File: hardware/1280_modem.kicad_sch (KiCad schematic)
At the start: 73 parts, among them IC1 SX1281IMLTRT, IC2 SKY65383-11, IC3 TJA1462AT_0Z, J2 Conn_Coaxial, J2 jst gh 4, J5 jst gh 6, J8 USB_C_Receptacle_USB2.0, J9 jst_sh 6, U13 STM32U575CGTx, U2 TPS7A20285PDBVR, U2 USBLC6-2SC6, Y1 48MHz, Y1 52MHz

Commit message: improvements
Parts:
- added C30, C31: 1u, Capacitor_SMD:C_0603_1608Metric, symbol Device:C_Small
- added D4: MBR1020VL, Diode_SMD:D_SOD-323_HandSoldering, symbol Device:D_Small
- added D5, D6, D7, D8: SZNUP2105L, Package_TO_SOT_SMD:SOT-23, symbol Power_Protection:SZNUP2105L
- added JP1: SolderJumper_2_Open, Jumper:SolderJumper-2_P1.3mm_Open_TrianglePad1.0x1.5mm, symbol Jumper:SolderJumper_2_Open
- added U4: TPS7A2450DBVR, Package_TO_SOT_SMD:SOT-23-5, symbol Regulator_Linear:TPS7A0525PDBV
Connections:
- net +5V: now also C31.1, U4.5 (OUT); no longer C2.2, C5.1, J2.1 (Pin_1), J5.1 (Pin_1), J8.A4 (VBUS), J8.A9 (VBUS), J8.B4 (VBUS), J8.B9 (VBUS), PS1.1 (VIN_1), PS1.2 (VIN_2), PS1.3 (EN), U2.5 (VBUS)
- net CAN_H: now also D5.2 (K)
- net CAN_L: now also D5.1 (K), JP1.2 (B); no longer R18.2
- net Earth: now also C30.1, C31.2, D5.3 (A), D6.3 (A), D7.3 (A), D8.3 (A), U4.2 (GND)
- net UART_CTS: now also D7.2 (K)
- net UART_RTS: now also D7.1 (K)
- net UART_RX: now also D6.1 (K)
- net UART_TX: now also D6.2 (K)
- new net: JP1.1 (A), R18.2
- new net VBUS: D4.2 (A), J8.A4 (VBUS), J8.A9 (VBUS), J8.B4 (VBUS), J8.B9 (VBUS), U2.5 (VBUS)
- new net VCC: C2.2, C30.2, C5.1, D4.1 (K), D8.1 (K), D8.2 (K), J2.1 (Pin_1), J5.1 (Pin_1), PS1.1 (VIN_1), PS1.2 (VIN_2), PS1.3 (EN), U4.1 (IN), U4.3 (EN)
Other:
- note added: "USB in -> 5.2v diode drop -> 4.9v ldo drop -> 4.7v"
- moved on the sheet: D1, D2, IC3, R11, R12, R18

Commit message: stuff
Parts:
- removed D3: pwr, LED_SMD:LED_0805_2012Metric, symbol Device:LED_Small
- removed R13: 330, Resistor_SMD:R_0603_1608Metric, symbol Device:R_Small
- added D9: IN-S128TATRGB, LED_SMD:LED_RGB_1210, symbol Device:LED_ARGB
- added R19: 330, Resistor_SMD:R_0603_1608Metric, symbol Device:R_Small
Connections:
- net +3V3: now also R19.2
- net Earth: now also D9.2 (RK)
- net LED_G: now reaches U13.20 (PB2)
- net LED_G: now also D9.3 (GK)
- net LED_B: now reaches U13.27 (PB14)
- net LED_B: now also D9.4 (BK)
- new net: D9.1 (A), R19.1
- no-connect marks 16 -> 14

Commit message: prettier schematic
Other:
- note added: "CONNECTORS"
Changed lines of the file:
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@@
     (fill (type none))
   )
-  (rectangle (start 19.05 180.34) (end 139.7 279.4)
+  (rectangle (start 19.05 180.34) (end 147.32 279.4)
     (stroke (width 0) (type default))
     (fill (type none))
@@
     (effects (font (size 1.27 1.27)) (justify left bottom))
   )
-  (text "CAN" (at 349.25 74.93 0)
+  (text "CONNECTORS" (at 349.25 74.93 0)
     (effects (font (size 1.27 1.27)) (justify left bottom))
   )

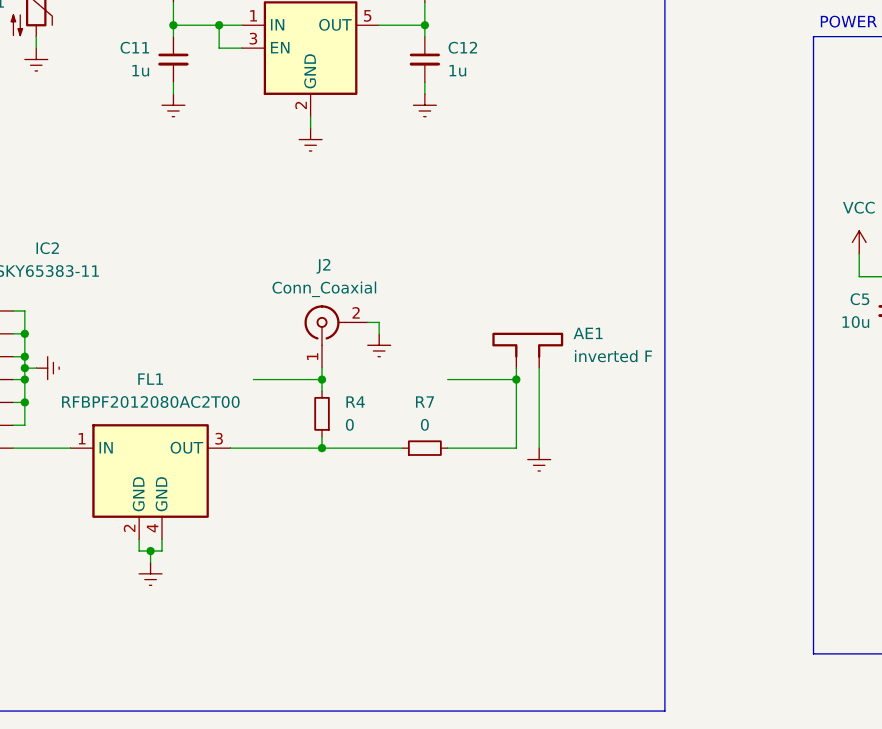
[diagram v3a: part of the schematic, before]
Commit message: micro strip and antenna tuning
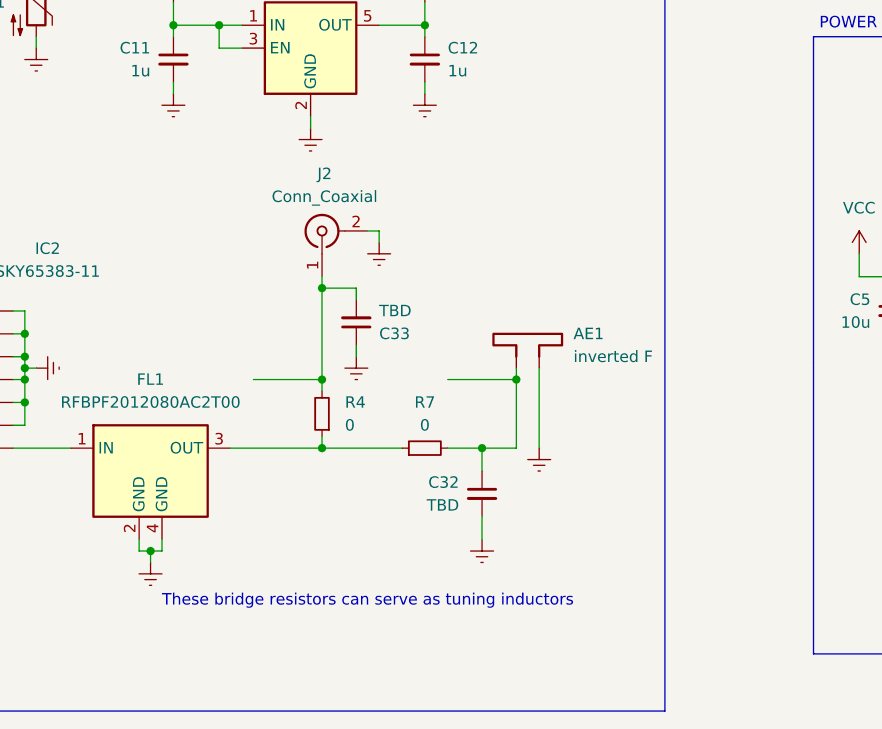
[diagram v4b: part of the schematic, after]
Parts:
- added C32, C33: TBD, Capacitor_SMD:C_0402_1005Metric, symbol Device:C_Small
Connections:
- net Earth: now also C32.2, C33.1
- net at AE1.1, R7.2: now also C32.1
- net at J2.1 (In), R4.2: now also C33.2
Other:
- note added: "These bridge resistors can serve as tuning inductors"
- moved on the sheet: J2
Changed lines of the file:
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@@
   (junction (at 22.86 198.12) (diameter 0) (color 0 0 0 0)
   )
+  (junction (at 127 250.19) (diameter 0) (color 0 0 0 0)
+  )
   (junction (at 69.85 119.38) (diameter 0) (color 0 0 0 0)
   )
+  (junction (at 109.22 232.41) (diameter 0) (color 0 0 0 0)
+  )
   (junction (at 76.2 240.03) (diameter 0) (color 0 0 0 0)
   )
@@
     (stroke (width 0) (type default))
   )
+  (wire (pts (xy 127 250.19) (xy 127 252.73))
+    (stroke (width 0) (type default))
+  )
   (wire (pts (xy 24.13 273.05) (xy 24.13 271.78))
     (stroke (width 0) (type default))
@@
     (stroke (width 0) (type default))
   )
+  (wire (pts (xy 109.22 232.41) (xy 113.03 232.41))
+    (stroke (width 0) (type default))
+  )
   (wire (pts (xy 120.65 203.2) (xy 120.65 204.47))
     (stroke (width 0) (type default))
@@
     (stroke (width 0) (type default))
   )
+  (wire (pts (xy 109.22 232.41) (xy 109.22 242.57))
+    (stroke (width 0) (type default))
+  )
   (wire (pts (xy 177.8 149.86) (xy 177.8 147.32))
     (stroke (width 0) (type default))
@@
     (stroke (width 0) (type default))
   )
-  (wire (pts (xy 109.22 241.3) (xy 109.22 242.57))
+  (wire (pts (xy 109.22 231.14) (xy 109.22 232.41))
     (stroke (width 0) (type default))
   )
@@
     (stroke (width 0) (type default))
   )
+  (wire (pts (xy 127 250.19) (xy 130.81 250.19))
+    (stroke (width 0) (type default))
+  )
   (wire (pts (xy 231.14 241.3) (xy 233.68 241.3))
     (stroke (width 0) (type default))
@@
     (stroke (width 0) (type default))
   )
+  (wire (pts (xy 127 257.81) (xy 127 260.35))
+    (stroke (width 0) (type default))
+  )
   (wire (pts (xy 364.49 46.99) (xy 373.38 46.99))
     (stroke (width 0) (type default))
@@
     (stroke (width 0) (type default))
   )
+  (wire (pts (xy 113.03 233.68) (xy 113.03 232.41))
+    (stroke (width 0) (type default))
+  )
   (wire (pts (xy 220.98 101.6) (xy 236.22 101.6))
     (stroke (width 0) (type default))
@@
     (stroke (width 0) (type default))
   )
-  (wire (pts (xy 123.19 250.19) (xy 130.81 250.19))
+  (wire (pts (xy 123.19 250.19) (xy 127 250.19))
     (stroke (width 0) (type default))
   )
@@
     (stroke (width 0) (type default))
   )
-  (wire (pts (xy 114.3 236.22) (xy 115.57 236.22))
+  (wire (pts (xy 114.3 226.06) (xy 115.57 226.06))
     (stroke (width 0) (type default))
   )
@@
     (stroke (width 0) (type default))
   )
-  (wire (pts (xy 115.57 236.22) (xy 115.57 237.49))
+  (wire (pts (xy 115.57 226.06) (xy 115.57 227.33))
     (stroke (width 0) (type default))
   )
@@
     (stroke (width 0) (type default))
   )
+  (wire (pts (xy 113.03 238.76) (xy 113.03 240.03))
+    (stroke (width 0) (type default))
+  )
   (wire (pts (xy 71.12 118.11) (xy 71.12 119.38))
     (stroke (width 0) (type default))
@@
     (effects (font (size 1.27 1.27)) (justify left bottom))
   )
+  (text "These bridge resistors can serve as tuning inductors"
+    (at 91.44 267.97 0)
+    (effects (font (size 1.27 1.27)) (justify left bottom))
+  )
   (text "Frontend" (at 182.88 199.39 0)
     (effects (font (size 1.27 1.27)) (justify left bottom))
@@
     )
   )
-  (symbol (lib_name "Earth_20") (lib_id "power:Earth") (at 115.57 237.49 0) (unit 1)
+  (symbol (lib_name "Earth_20") (lib_id "power:Earth") (at 115.57 227.33 0) (unit 1)
     (in_bom yes) (on_board yes) (dnp no) (fields_autoplaced)
-    (property "Reference" "#PWR035" (at 115.57 243.84 0)
+    (property "Reference" "#PWR035" (at 115.57 233.68 0)
       (effects (font (size 1.27 1.27)) hide)
     )
-    (property "Value" "Earth" (at 115.57 241.3 0)
+    (property "Value" "Earth" (at 115.57 231.14 0)
       (effects (font (size 1.27 1.27)) hide)
     )
-    (property "Footprint" "" (at 115.57 237.49 0)
+    (property "Footprint" "" (at 115.57 227.33 0)
       (effects (font (size 1.27 1.27)) hide)
     )
-    (property "Datasheet" "~" (at 115.57 237.49 0)
+    (property "Datasheet" "~" (at 115.57 227.33 0)
       (effects (font (size 1.27 1.27)) hide)
     )
@@
     )
   )
+  (symbol (lib_id "Device:C_Small") (at 127 255.27 0) (mirror y) (unit 1)
+    (in_bom yes) (on_board yes) (dnp no)
+    (property "Reference" "C32" (at 124.46 254.0063 0)
+      (effects (font (size 1.27 1.27)) (justify left))
+    )
+    (property "Value" "TBD" (at 124.46 256.5463 0)
+      (effects (font (size 1.27 1.27)) (justify left))
+    )
+    (property "Footprint" "Capacitor_SMD:C_0402_1005Metric" (at 127 255.27 0)
+      (effects (font (size 1.27 1.27)) hide)
+    )
+    (property "Datasheet" "~" (at 127 255.27 0)
+      (effects (font (size 1.27 1.27)) hide)
+    )
+    (pin "1")
+    (pin "2")
+    (instances
+      (project "1280_modem"
+        (path "/f19b1dac-2dd5-424b-bd9e-1e3b3f325373"
+          (reference "C32") (unit 1)
+        )
+      )
+    )
+  )
   (symbol (lib_id "power:+3.3VA") (at 41.91 264.16 0) (unit 1)
     (in_bom yes) (on_board yes) (dnp no) (fields_autoplaced)
@@
     )
   )
+  (symbol (lib_name "Earth_44") (lib_id "power:Earth") (at 113.03 240.03 0) (unit 1)
+    (in_bom yes) (on_board yes) (dnp no) (fields_autoplaced)
+    (property "Reference" "#PWR084" (at 113.03 246.38 0)
+      (effects (font (size 1.27 1.27)) hide)
+    )
+    (property "Value" "Earth" (at 113.03 243.84 0)
+      (effects (font (size 1.27 1.27)) hide)
+    )
+    (property "Footprint" "" (at 113.03 240.03 0)
+      (effects (font (size 1.27 1.27)) hide)
+    )
+    (property "Datasheet" "~" (at 113.03 240.03 0)
+      (effects (font (size 1.27 1.27)) hide)
+    )
+    (pin "1")
+    (instances
+      (project "1280_modem"
+        (path "/f19b1dac-2dd5-424b-bd9e-1e3b3f325373"
+          (reference "#PWR084") (unit 1)
+        )
+      )
+    )
+  )
   (symbol (lib_name "Earth_12") (lib_id "power:Earth") (at 350.52 205.105 0) (unit 1)
     (in_bom yes) (on_board yes) (dnp no) (fields_autoplaced)
@@
     )
   )
+  (symbol (lib_id "Device:C_Small") (at 113.03 236.22 0) (mirror x) (unit 1)
+    (in_bom yes) (on_board yes) (dnp no)
+    (property "Reference" "C33" (at 115.57 237.4837 0)
+      (effects (font (size 1.27 1.27)) (justify left))
+    )
+    (property "Value" "TBD" (at 115.57 234.9437 0)
+      (effects (font (size 1.27 1.27)) (justify left))
+    )
+    (property "Footprint" "Capacitor_SMD:C_0402_1005Metric" (at 113.03 236.22 0)
+      (effects (font (size 1.27 1.27)) hide)
+    )
+    (property "Datasheet" "~" (at 113.03 236.22 0)
+      (effects (font (size 1.27 1.27)) hide)
+    )
+    (pin "1")
+    (pin "2")
+    (instances
+      (project "1280_modem"
+        (path "/f19b1dac-2dd5-424b-bd9e-1e3b3f325373"
+          (reference "C33") (unit 1)
+        )
+      )
+    )
+  )
   (symbol (lib_name "Earth_18") (lib_id "power:Earth") (at 113.03 100.33 0) (unit 1)
     (in_bom yes) (on_board yes) (dnp no) (fields_autoplaced)
@@
     )
   )
+  (symbol (lib_name "Earth_43") (lib_id "power:Earth") (at 127 260.35 0) (unit 1)
+    (in_bom yes) (on_board yes) (dnp no) (fields_autoplaced)
+    (property "Reference" "#PWR011" (at 127 266.7 0)
+      (effects (font (size 1.27 1.27)) hide)
+    )
+    (property "Value" "Earth" (at 127 264.16 0)
+      (effects (font (size 1.27 1.27)) hide)
+    )
+    (property "Footprint" "" (at 127 260.35 0)
+      (effects (font (size 1.27 1.27)) hide)
+    )
+    (property "Datasheet" "~" (at 127 260.35 0)
+      (effects (font (size 1.27 1.27)) hide)
+    )
+    (pin "1")
+    (instances
+      (project "1280_modem"
+        (path "/f19b1dac-2dd5-424b-bd9e-1e3b3f325373"
+          (reference "#PWR011") (unit 1)
+        )
+      )
+    )
+  )
   (symbol (lib_id "Mechanical:MountingHole_Pad") (at 127 59.69 0) (unit 1)
     (in_bom yes) (on_board yes) (dnp no) (fields_autoplaced)
@@
     )
   )
-  (symbol (lib_id "Connector:Conn_Coaxial") (at 109.22 236.22 90) (unit 1)
+  (symbol (lib_id "Connector:Conn_Coaxial") (at 109.22 226.06 90) (unit 1)
     (in_bom yes) (on_board yes) (dnp no) (fields_autoplaced)
-    (property "Reference" "J2" (at 109.5132 229.87 90)
+    (property "Reference" "J2" (at 109.5132 219.71 90)
       (effects (font (size 1.27 1.27)))
     )
-    (property "Value" "Conn_Coaxial" (at 109.5132 232.41 90)
+    (property "Value" "Conn_Coaxial" (at 109.5132 222.25 90)
       (effects (font (size 1.27 1.27)))
     )
-    (property "Footprint" "Connector_Coaxial:SMA_Amphenol_901-143_Horizontal" (at 109.22 236.22 0)
+    (property "Footprint" "Connector_Coaxial:SMA_Amphenol_901-143_Horizontal" (at 109.22 226.06 0)
       (effects (font (size 1.27 1.27)) hide)
     )
-    (property "Datasheet" " ~" (at 109.22 236.22 0)
+    (property "Datasheet" " ~" (at 109.22 226.06 0)
       (effects (font (size 1.27 1.27)) hide)
     )

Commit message: add pdf
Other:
- note added: "USB in -> 5.2v diode drop -> 4.9v ldo drop -> 4.7v works down to 4.5V"
- note removed: "USB in -> 5.2v diode drop -> 4.9v ldo drop -> 4.7v"
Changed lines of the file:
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@@
     (effects (font (size 1.27 1.27)) (justify left bottom))
   )
-  (text "USB in -> 5.2v\ndiode drop -> 4.9v\nldo drop -> 4.7v\n"
+  (text "USB in -> 5.2v\ndiode drop -> 4.9v\nldo drop -> 4.7v\nworks down to 4.5V"
     (at 180.34 173.99 0)
     (effects (font (size 1.27 1.27)) (justify left bottom))
